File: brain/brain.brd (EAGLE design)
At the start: 59.7 x 53.3 mm, 4 parts

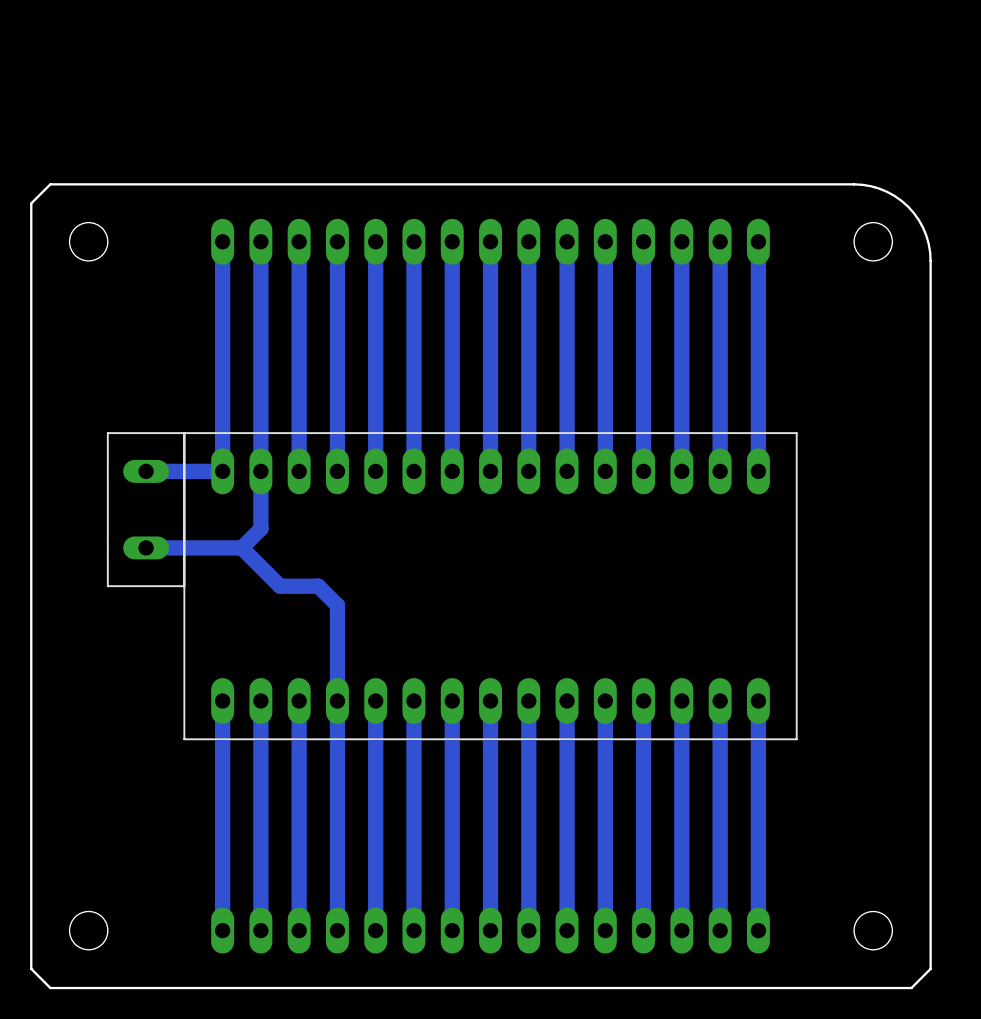
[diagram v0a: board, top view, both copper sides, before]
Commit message: Added decoupling capacitors to brain board. Also adjusted the origin to be in the bottom left corner of the PCB.
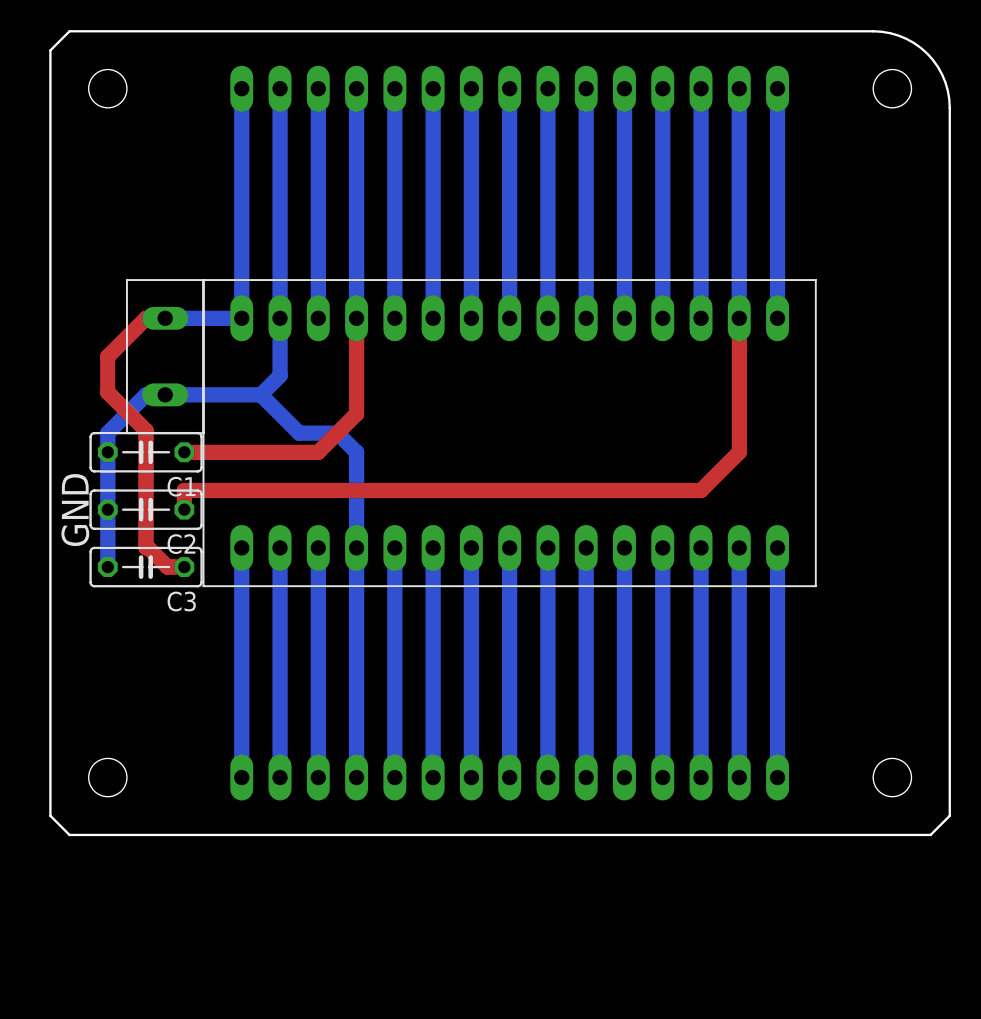
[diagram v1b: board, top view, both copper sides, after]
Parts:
- added C1, C2, C3: (no value), rcl:C050-025X075
- moved U$5 10.2 mm to (30.5, 49.5)
- moved U$1 10.2 mm to (30.5, 19.1)
- moved U$2 10.2 mm to (30.5, 3.81)
- moved U$3 10.2 mm to (7.62, 31.8)
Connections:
- removed net 3V3: U$1.3V3, U$5.3V3
- removed net 5V: U$1.5V, U$5.5V
- removed net VIN: U$1.VIN, U$3.POS, U$5.VIN
- new net +3V3: C2.1, U$1.3V3, U$5.3V3
- new net +5V: C1.1, U$1.5V, U$5.5V
- new net V+: C3.1, U$1.VIN, U$3.POS, U$5.VIN
- net GND: now also C1.2, C2.2, C3.2
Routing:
- net +3V3: track 0.00 -> 63.3 mm
- net V+: track 0.00 -> 42.0 mm
- net +5V: track 0.00 -> 34.1 mm
- net VIN: track 20.3 -> 0.00 mm
- net 5V: track 15.2 -> 0.00 mm
- net 3V3: track 15.2 -> 0.00 mm
- net GND: track 56.7 -> 70.5 mm
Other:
- board text added: "GND"
